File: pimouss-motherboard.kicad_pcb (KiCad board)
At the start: 4 copper layers, 281 parts, among them J1 Conn_02x10_Odd_Even, J10 Barrel_Jack_Switch, J2 TMS-105-57-GD, J3 Conn_02x10_Odd_Even, J4 Conn_01x03_Male, J5 Micro_SD_Card_Det, J9 RJSAE-5x8, P1 QSH-060-01-L-D-A, P2 PCIE-064-02, P3 MPCIE-Socket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

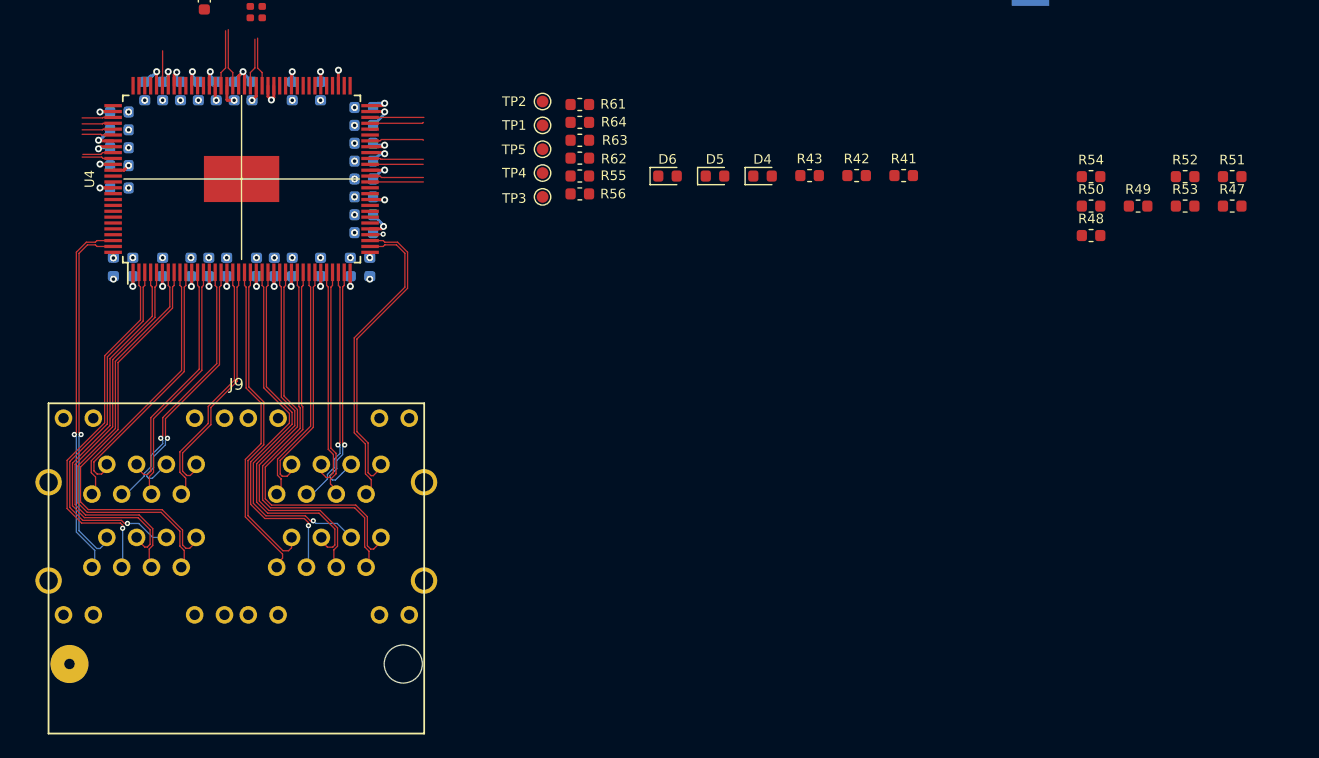
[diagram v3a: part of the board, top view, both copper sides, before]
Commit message: pcb: Put RJ jacks closer to PHY and wire PHY LEDs
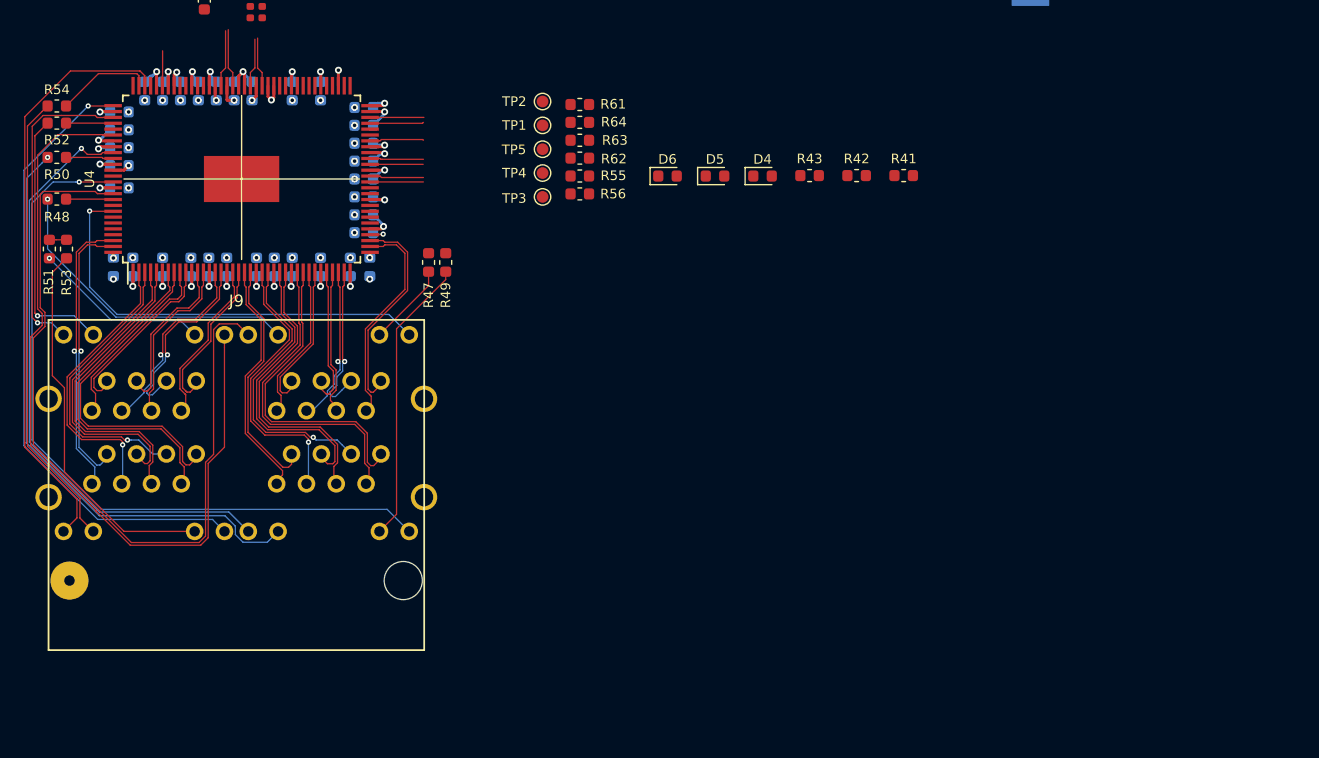
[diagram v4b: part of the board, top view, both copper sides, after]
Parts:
- moved R51 101.0 mm to (22.2, 130.2), turned to 270 degrees
- moved R52 96.3 mm to (22.9, 119.4), turned to 180 degrees
- moved R53 95.4 mm to (23.7, 130.2), turned to 270 degrees
- moved R54 88.4 mm to (22.9, 118.0), turned to 180 degrees
- moved R50 88.3 mm to (22.9, 122.4), turned to 180 degrees
- moved R48 88.2 mm to (22.9, 125.9), turned to 180 degrees
- moved R47 68.7 mm to (54.5, 131.3), turned to 270 degrees
- moved R49 59.2 mm to (56.0, 131.3), turned to 270 degrees
- moved J9 7.11 mm to (38.2, 158.4)
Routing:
- net /LED_P3_0: track 0.00 -> 68.1 mm
- net /phy_data/LED_P1_3: track 2.67 -> 69.3 mm
- net /phy_data/LED_P2_3: track 0.00 -> 63.2 mm, vias 0 -> 1
- net /phy_data/LED_P0_3: track 0.00 -> 53.5 mm, vias 0 -> 1
- net Net-(J9-PadB11): track 0.00 -> 50.8 mm, vias 0 -> 1
- net /phy_data/LED_P0_0: track 0.00 -> 50.5 mm
- net /phy_data/LED_P2_0: track 2.64 -> 51.6 mm, vias 0 -> 1
- net Net-(J9-PadD11): track 0.00 -> 39.3 mm
- net /phy_data/LED_P3_3: track 0.00 -> 37.4 mm, vias 0 -> 1
- net Net-(J9-PadD10): track 0.00 -> 32.3 mm
- net Net-(J9-PadA11): track 0.00 -> 26.9 mm, vias 0 -> 1
- net Net-(J9-PadB10): track 0.00 -> 24.5 mm
- net /phy_data/LED_P1_0: track 2.66 -> 26.9 mm, vias 0 -> 1
- net Net-(J9-PadC11): track 0.00 -> 22.4 mm, vias 0 -> 1
- net Net-(J9-PadC10): track 0.00 -> 15.1 mm, vias 0 -> 1
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
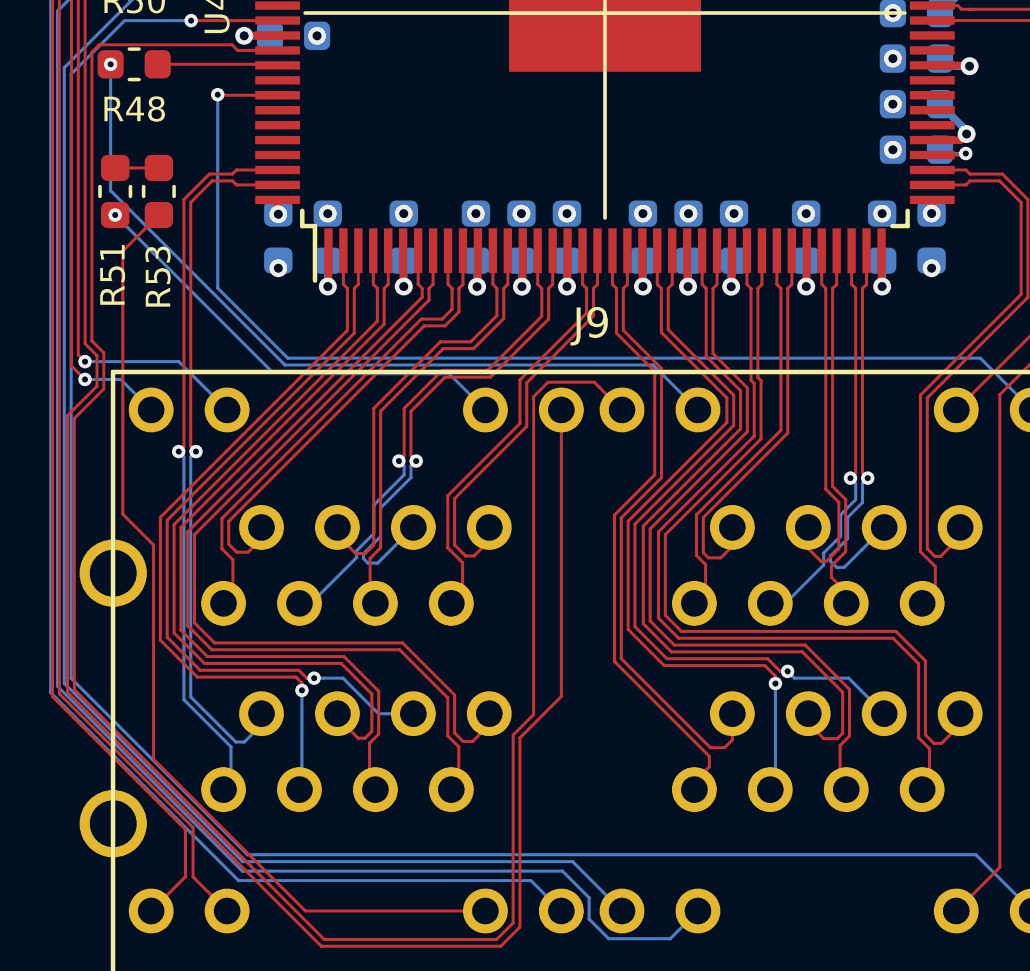
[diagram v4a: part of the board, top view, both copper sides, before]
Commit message: pcb: Tune RJ45 diff lanes
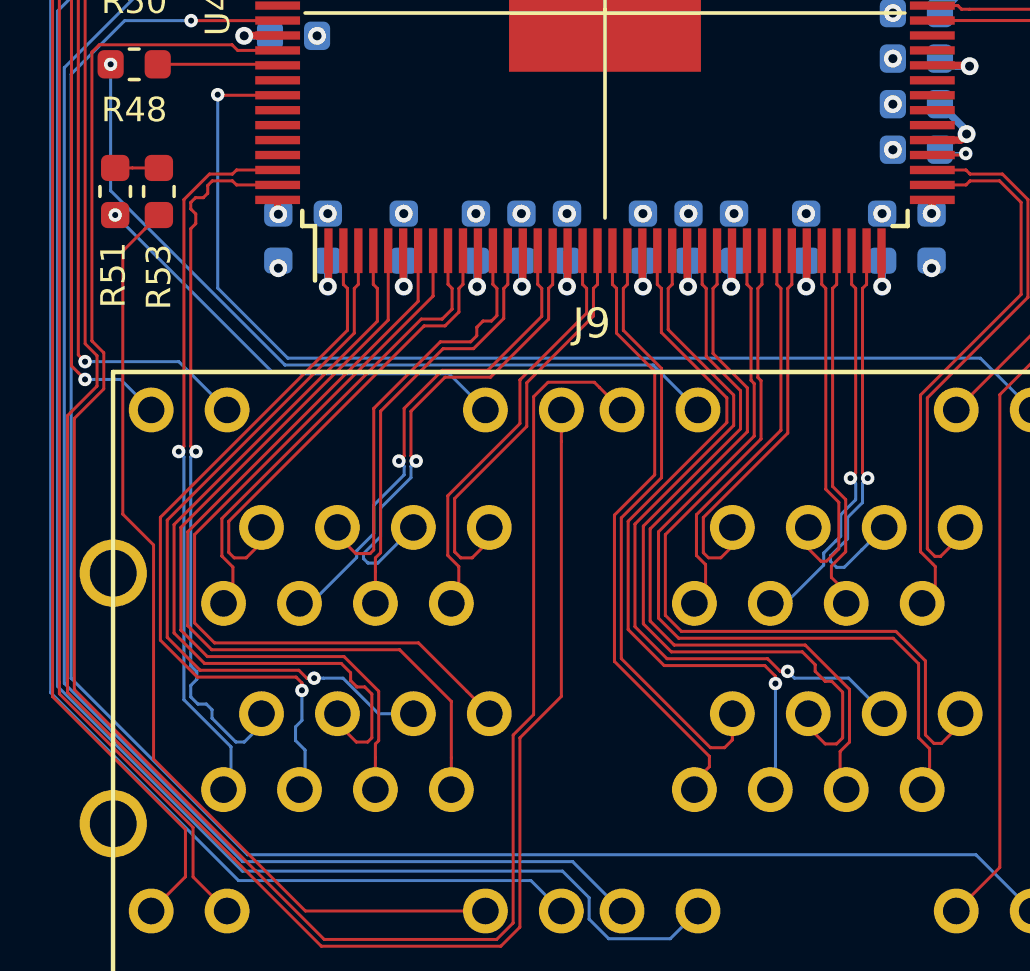
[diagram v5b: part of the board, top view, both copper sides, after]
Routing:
- net /phy_data/MDIP0_3_N: track 28.6 -> 26.9 mm
- net /phy_data/MDIP0_0_N: track 23.3 -> 23.9 mm

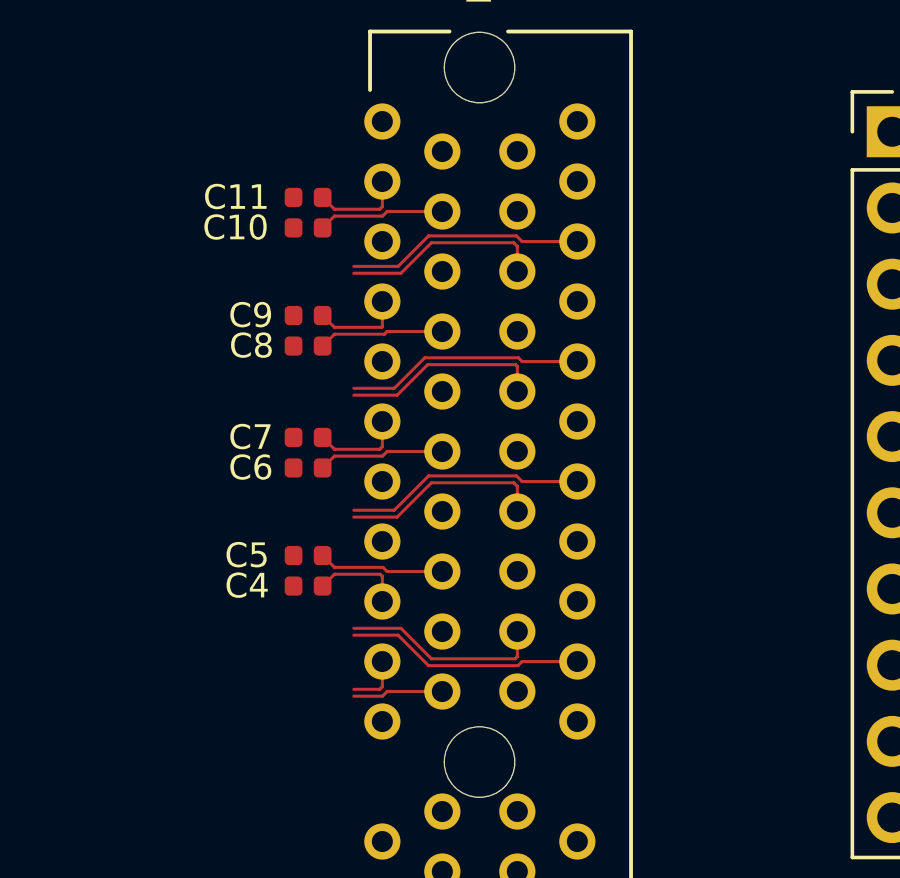
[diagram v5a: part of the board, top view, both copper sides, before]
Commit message: pcb: Rework PCIe X4 connector fanout
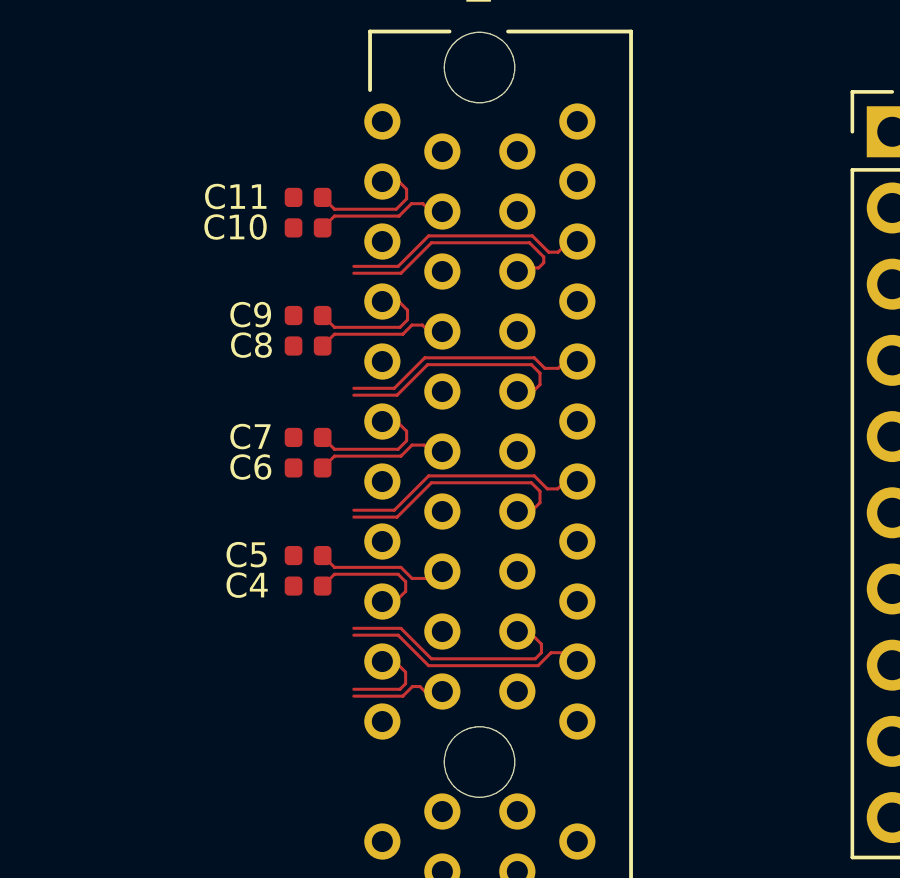
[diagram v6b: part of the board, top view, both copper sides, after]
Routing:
- net /PCIE_X4_TX3_P: track 6.76 -> 8.14 mm
- net /pcie/X4_R2_N: track 3.00 -> 4.38 mm
- net /pcie/X4_R1_N: track 3.03 -> 4.34 mm
- net /pcie/X4_R3_N: track 3.03 -> 4.34 mm
- net /PCIE_X4_CLK_N: track 1.83 -> 3.11 mm
- net /PCIE_X4_TX0_N: track 6.74 -> 8.02 mm
- net /pcie/X4_R0_P: track 3.02 -> 4.27 mm
- net /PCIE_X4_TX2_P: track 6.73 -> 7.97 mm
- net /PCIE_X4_TX1_P: track 6.81 -> 8.05 mm

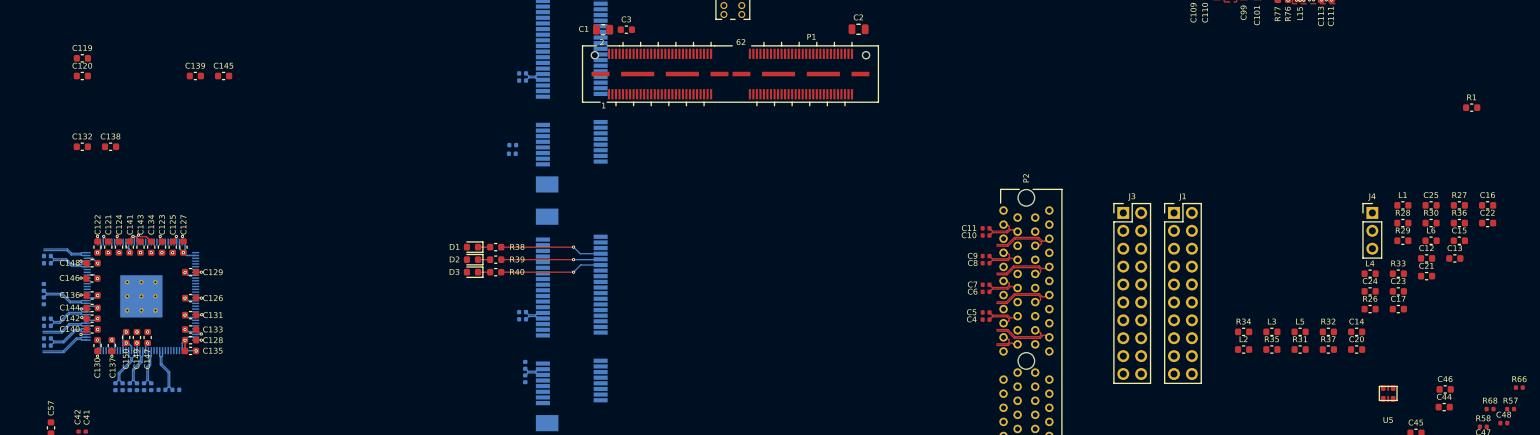
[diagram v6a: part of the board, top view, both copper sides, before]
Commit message: pcb: Add PCIe switch power wiring
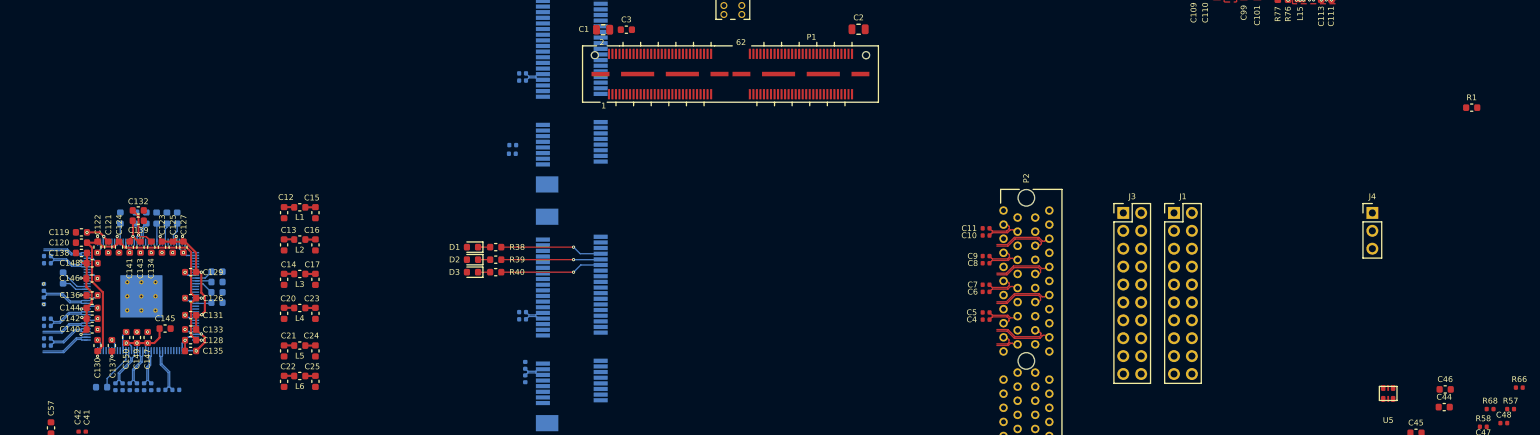
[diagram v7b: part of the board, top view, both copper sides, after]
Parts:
- R26, R27, R28, R29, R30, R31, R32, R33, R34, R35, R36, R37: moved to B.Cu
- moved R27 194.4 mm to (42.6, 103.2), turned to 180 degrees
- moved R26 185.6 mm to (37.1, 87.7), turned to 270 degrees
- moved R36 183.4 mm to (51.9, 79.2), turned to 270 degrees
- moved R33 179.3 mm to (47.5, 79.2), turned to 270 degrees
- moved R28 174.0 mm to (53.3, 79.2), turned to 90 degrees
- moved R30 172.5 mm to (59.0, 88.3), turned to 180 degrees
- moved C22 172.3 mm to (68.5, 102.4), turned to 270 degrees
- moved R32 172.2 mm to (45.3, 79.2), turned to 270 degrees
- moved R29 168.4 mm to (59.0, 86.8), turned to 180 degrees
- moved C16 166.5 mm to (73.0, 83.0), turned to 270 degrees
- moved C13 166.2 mm to (68.5, 83.0), turned to 270 degrees
- moved C21 162.5 mm to (68.5, 98.0), turned to 270 degrees
- moved C15 162.4 mm to (73.0, 78.4), turned to 270 degrees
- moved C12 162.3 mm to (68.5, 78.4), turned to 270 degrees
- moved L6 161.7 mm to (70.7, 101.6)
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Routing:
- net /pcie/switch/VDDC: track 15.1 -> 68.1 mm, vias 9 -> 10
- net /pcie/switch/VDDR: track 7.90 -> 55.4 mm
- net /pcie/switch/AVDDH: track 4.95 -> 23.1 mm
- net /pcie/switch/AVDD: track 8.65 -> 21.6 mm
- net /pcie/switch/CVDDR: track 3.83 -> 11.6 mm
- net Net-(R27-Pad1): track 0.00 -> 6.29 mm
- net +1V0: track 0.00 -> 4.34 mm
- net +3V3: track 13.4 -> 17.7 mm
- net Net-(R26-Pad1): track 0.00 -> 4.24 mm
- net Net-(R26-Pad2): track 0.00 -> 3.75 mm
- net Net-(R33-Pad2): track 0.00 -> 3.03 mm
- net /pcie/switch/VDDCAUX: track 4.91 -> 7.90 mm
- net Net-(R28-Pad1): track 0.00 -> 2.87 mm
- net Net-(R34-Pad2): track 0.00 -> 2.85 mm
- net Net-(R31-Pad2): track 0.00 -> 2.75 mm
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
